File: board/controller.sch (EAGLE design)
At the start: 70 parts, among them J1 X, J10 FEED_HOLD, J11 PROBE, J12 ERROR, J13 HOLDING, J14 GND, J15 MOTOR_CURRENT, J16 SD_READER, J17 WHEEL, J18 FEED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

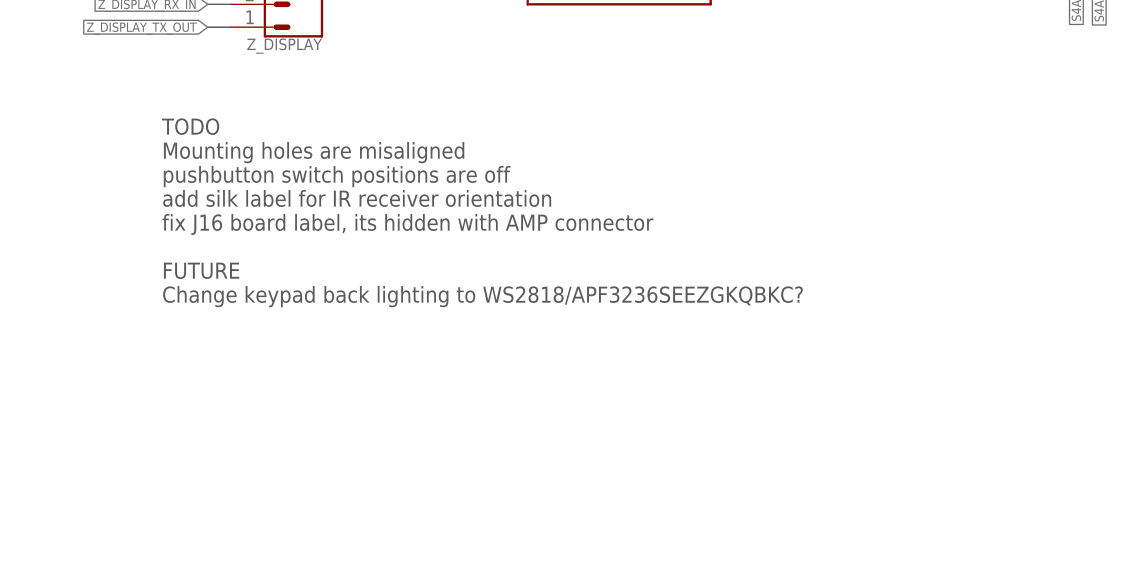
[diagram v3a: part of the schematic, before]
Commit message: feedoverride now functional
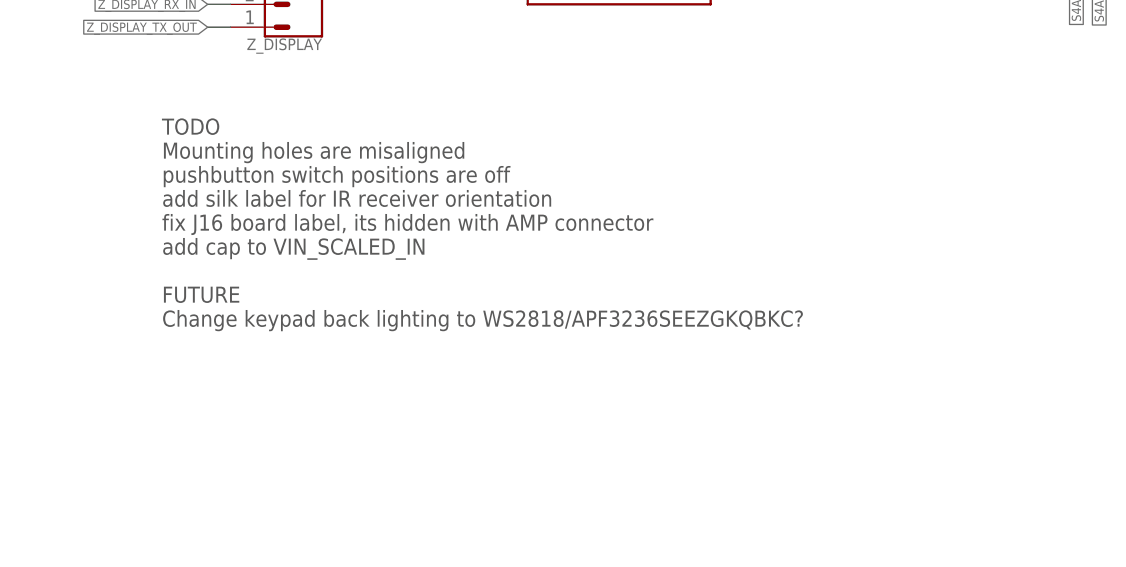
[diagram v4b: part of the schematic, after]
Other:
- note added: "TODO Mounting holes are misaligned pushbutton switch positions are off add silk label for IR receiver orientation fix J16 board label, its hidden with AMP connector add cap to VIN_SCALED_IN FUTURE Change keypad back lighting to WS2818/APF3236SEEZGKQBKC?"
- note removed: "TODO Mounting holes are misaligned pushbutton switch positions are off add silk label for IR receiver orientation fix J16 board label, its hidden with AMP connector FUTURE Change keypad back lighting to WS2818/APF3236SEEZGKQBKC?"
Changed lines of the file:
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@@
 add silk label for IR receiver orientation
 fix J16 board label, its hidden with AMP connector
+add cap to VIN_SCALED_IN
 FUTURE
 Change keypad back lighting to WS2818/APF3236SEEZGKQBKC?</text>

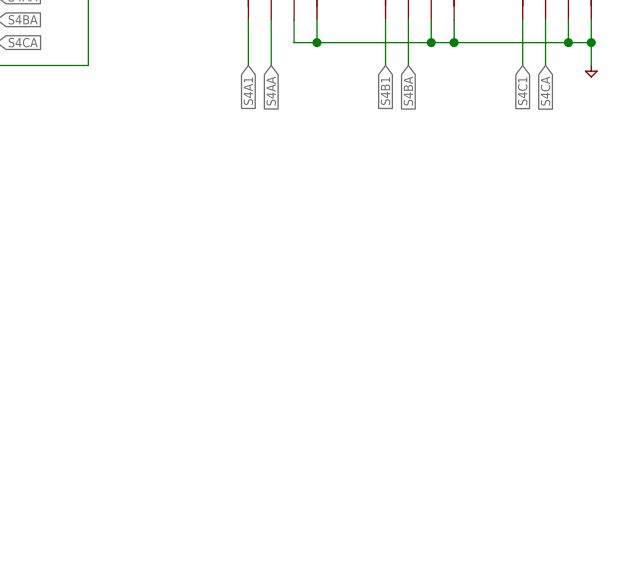
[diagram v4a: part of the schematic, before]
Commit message: added v1.0 to v1.1 notes
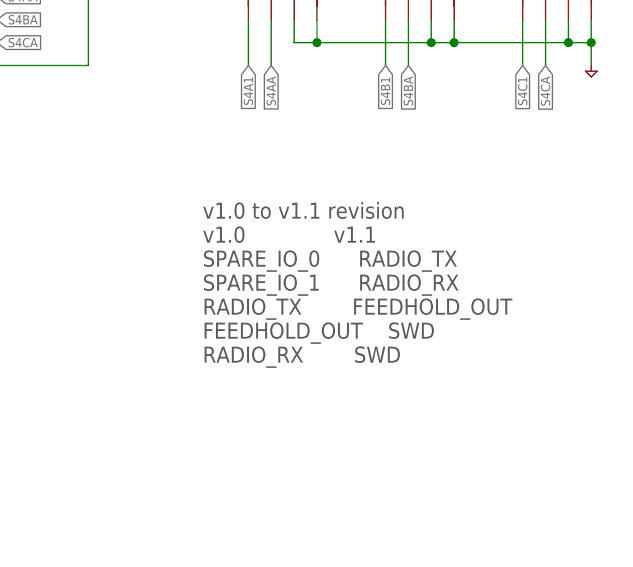
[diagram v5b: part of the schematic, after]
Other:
- note added: "v1.0 to v1.1 revision v1.0 v1.1 SPARE_IO_0 RADIO_TX SPARE_IO_1 RADIO_RX RADIO_TX FEEDHOLD_OUT FEEDHOLD_OUT SWD RADIO_RX SWD"
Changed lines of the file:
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@@
 <text x="93.98" y="155.448" size="1.016" layer="97" align="top-left">1.1 and 1.0 are used
 for 059's SWD pins</text>
+<text x="228.6" y="91.44" size="1.778" layer="97" font="fixed" align="top-left">v1.0 to v1.1 revision
+v1.0              v1.1
+SPARE_IO_0      RADIO_TX
+SPARE_IO_1      RADIO_RX
+RADIO_TX        FEEDHOLD_OUT
+FEEDHOLD_OUT    SWD
+RADIO_RX        SWD
+</text>
 </plain>
 <instances>

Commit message: don't know what changes are
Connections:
- new net MISC_ENABLE_OUT: J5.3
- net STEPPER_ENABLE_OUT: no longer J5.3
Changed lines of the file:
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@@
 <net name="STEPPER_ENABLE_OUT" class="0">
-<segment>
-<pinref part="J5" gate="G$1" pin="3"/>
-<wire x1="15.24" y1="144.78" x2="17.78" y2="144.78" width="0.1524" layer="91"/>
-<label x="17.78" y="144.78" size="1.016" layer="95" xref="yes"/>
-</segment>
 <segment>
 <pinref part="U2" gate="G$1" pin="P0_4"/>
@@
 </segment>
 </net>
+<net name="MISC_ENABLE_OUT" class="0">
+<segment>
+<pinref part="J5" gate="G$1" pin="3"/>
+<wire x1="15.24" y1="144.78" x2="17.78" y2="144.78" width="0.1524" layer="91"/>
+<label x="17.78" y="144.78" size="1.016" layer="95" xref="yes"/>
+</segment>
+</net>

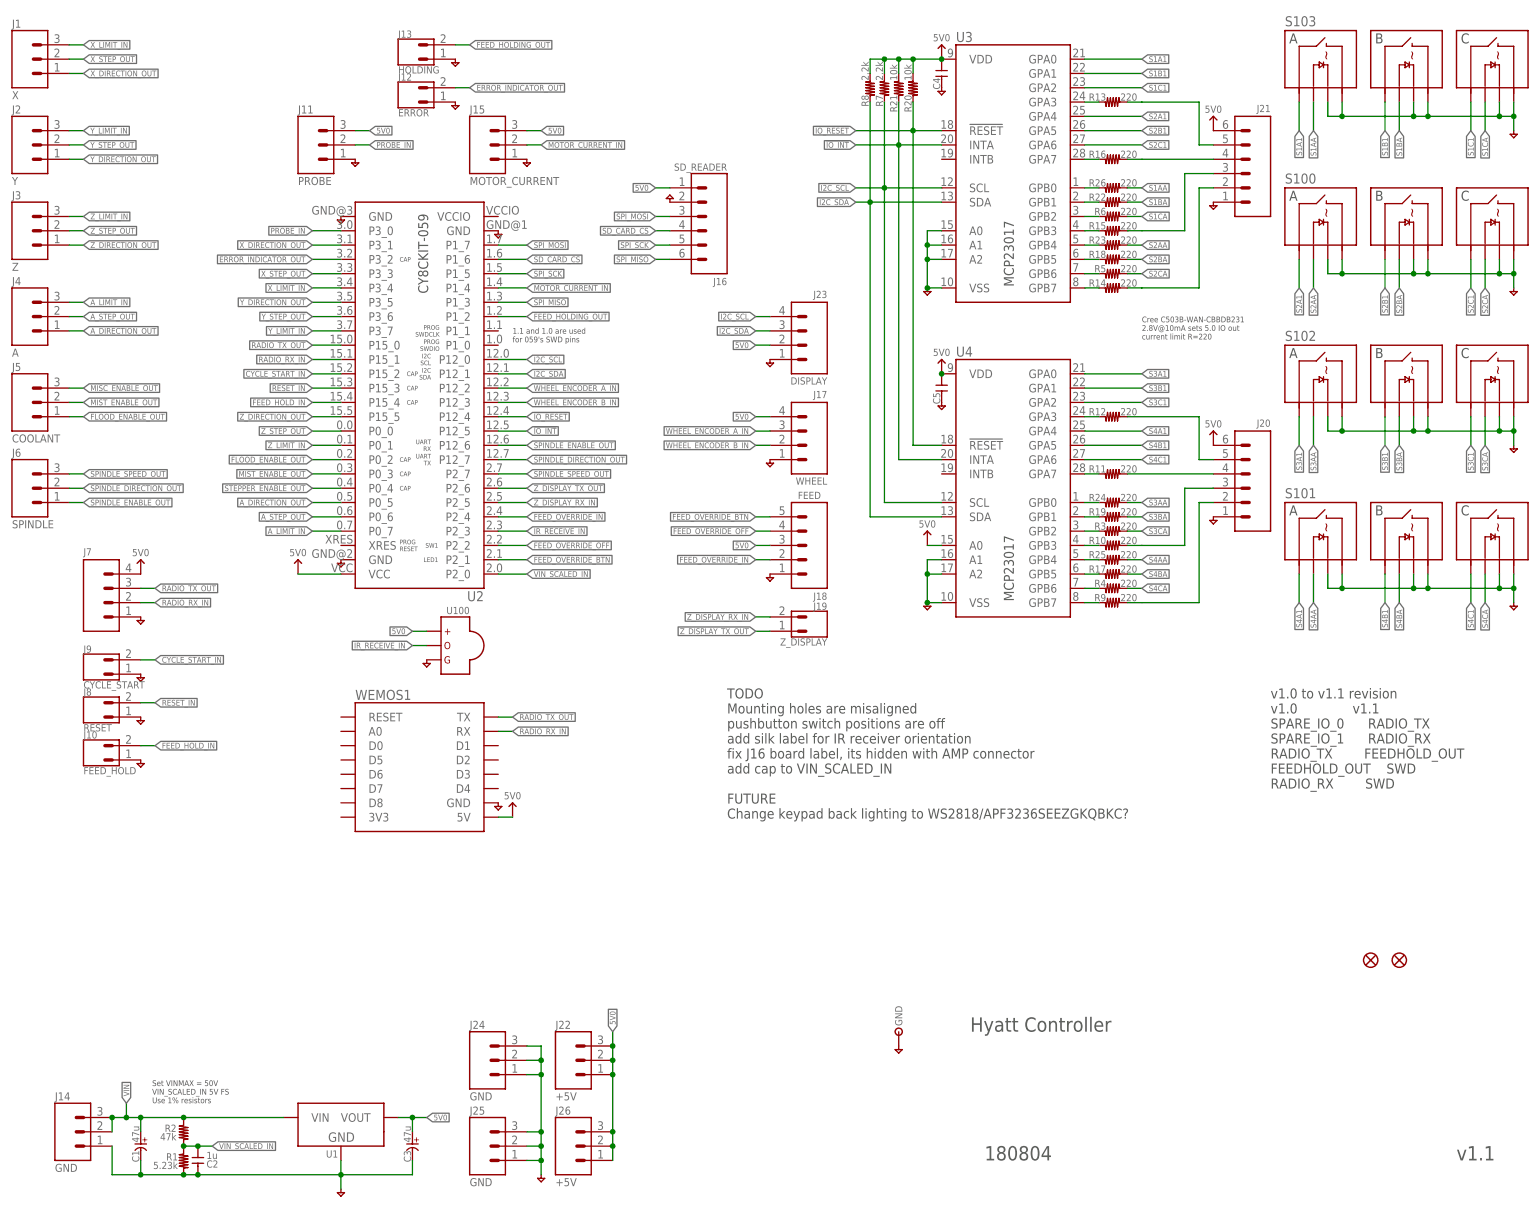
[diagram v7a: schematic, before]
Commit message: added currect limit resistors for holding and error control panel leds added alarm string to control panel display if in alarm state, hitting any control panel key clears alarm without reseting
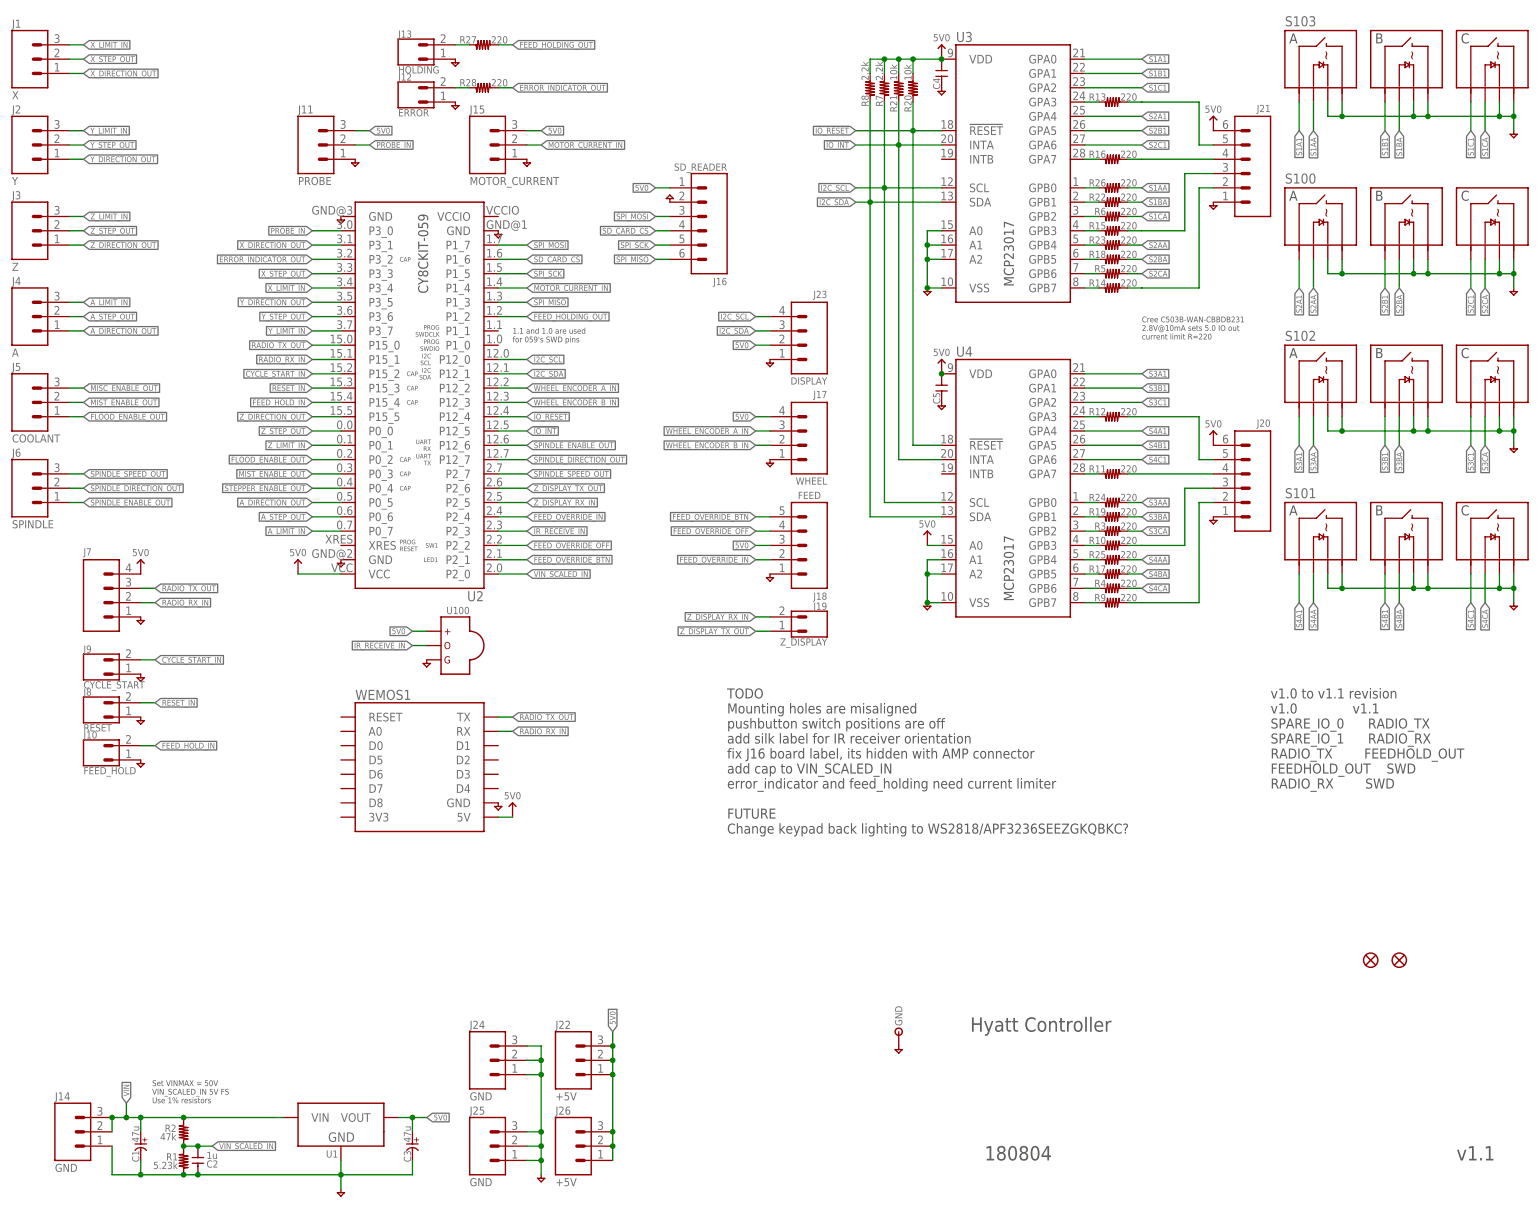
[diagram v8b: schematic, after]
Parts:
- added R27, R28: 220, holla:R-0603
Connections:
- new net N$12: J13.2, R27.1
- new net N$13: J12.2, R28.1
- net ERROR_INDICATOR_OUT: now also R28.2; no longer J12.2
- net FEED_HOLDING_OUT: now also R27.2; no longer J13.2
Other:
- note added: "TODO Mounting holes are misaligned pushbutton switch positions are off add silk label for IR receiver orientation fix J16 board label, its hidden with AMP connector add cap to VIN_SCALED_IN error_indicator and feed_holding need current limiter FUTURE Change keypad back lighting to WS2818/APF3236SEEZGKQBKC?"
- note removed: "TODO Mounting holes are misaligned pushbutton switch positions are off add silk label for IR receiver orientation fix J16 board label, its hidden with AMP connector add cap to VIN_SCALED_IN FUTURE Change keypad back lighting to WS2818/APF3236SEEZGKQBKC?"
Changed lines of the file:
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@@
 <setting verticaltext="up"/>
 </settings>
-<grid distance="0.1" unitdist="inch" unit="inch" style="lines" multiple="1" display="yes" altdistance="0.01" altunitdist="inch" altunit="inch"/>
+<grid distance="0.1" unitdist="inch" unit="inch" style="lines" multiple="1" display="no" altdistance="0.01" altunitdist="inch" altunit="inch"/>
 <layers>
 <layer number="1" name="Top" color="4" fill="1" visible="no" active="no"/>
@@
 <part name="J7" library="holla" deviceset="CONN-04" device="-0.1"/>
 <part name="J5" library="holla" deviceset="CONN-03" device="-3.81MM-PLUGIN-SCREW" value="COOLANT"/>
+<part name="R27" library="holla" deviceset="R" device="-0603" value="220"/>
+<part name="R28" library="holla" deviceset="R" device="-0603" value="220"/>
 </parts>
 <sheets>
@@
 fix J16 board label, its hidden with AMP connector
 add cap to VIN_SCALED_IN
+error_indicator and feed_holding need current limiter
 FUTURE
 Change keypad back lighting to WS2818/APF3236SEEZGKQBKC?</text>
@@
 <instance part="J7" gate="G$1" x="22.86" y="109.22"/>
 <instance part="J5" gate="G$1" x="10.16" y="142.24"/>
+<instance part="R27" gate="G$1" x="88.9" y="205.74"/>
+<instance part="R28" gate="G$1" x="88.9" y="198.12"/>
 </instances>
 <busses>
@@
 <net name="ERROR_INDICATOR_OUT" class="0">
 <segment>
-<pinref part="J12" gate="G$1" pin="2"/>
-<wire x1="83.82" y1="198.12" x2="86.36" y2="198.12" width="0.1524" layer="91"/>
-<label x="86.36" y="198.12" size="1.016" layer="95" xref="yes"/>
+<wire x1="91.44" y1="198.12" x2="93.98" y2="198.12" width="0.1524" layer="91"/>
+<label x="93.98" y="198.12" size="1.016" layer="95" xref="yes"/>
+<pinref part="R28" gate="G$1" pin="2"/>
 </segment>
 <segment>
@@
 <net name="FEED_HOLDING_OUT" class="0">
 <segment>
-<pinref part="J13" gate="G$1" pin="2"/>
-<wire x1="83.82" y1="205.74" x2="86.36" y2="205.74" width="0.1524" layer="91"/>
-<label x="86.36" y="205.74" size="1.016" layer="95" xref="yes"/>
+<wire x1="91.44" y1="205.74" x2="93.98" y2="205.74" width="0.1524" layer="91"/>
+<label x="93.98" y="205.74" size="1.016" layer="95" xref="yes"/>
+<pinref part="R27" gate="G$1" pin="2"/>
 </segment>
 <segment>
@@
 </segment>
 </net>
+<net name="N$12" class="0">
+<segment>
+<pinref part="J13" gate="G$1" pin="2"/>
+<pinref part="R27" gate="G$1" pin="1"/>
+<wire x1="86.36" y1="205.74" x2="83.82" y2="205.74" width="0.1524" layer="91"/>
+</segment>
+</net>
+<net name="N$13" class="0">
+<segment>
+<pinref part="J12" gate="G$1" pin="2"/>
+<pinref part="R28" gate="G$1" pin="1"/>
+<wire x1="86.36" y1="198.12" x2="83.82" y2="198.12" width="0.1524" layer="91"/>
+</segment>
+</net>
